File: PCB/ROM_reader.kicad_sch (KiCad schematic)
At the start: 37 parts, among them J1 TTL_UART, J2 USB_B_Mini, J3 ISP, U1 CH340G, U2 ATmega128A-A, Y1 12MHz

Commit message: ROM reader project PCBs updated
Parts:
- removed C11: 100u, Capacitor_SMD:CP_Elec_8x5.4, symbol Device:C_Polarized
- removed L1, L2: 100u, Inductor_SMD:L_1812_4532Metric_Pad1.30x3.40mm_HandSolder, symbol Device:L
- removed R5: 10M, Resistor_SMD:R_1206_3216Metric_Pad1.30x1.75mm_HandSolder, symbol Device:R
- added D1: Schottky, Diode_SMD:D_SMB_Handsoldering, symbol Device:D_Schottky
- added H1, H2, H3, H4: MH, MountingHole:MountingHole_3.2mm_M3_DIN965, symbol Mechanical:MountingHole
- added J4: EC, Connector_PinHeader_2.54mm:PinHeader_1x02_P2.54mm_Vertical, symbol Connector:Conn_01x02_Pin
- F1: footprint Fuse:Fuse_2010_5025Metric_Pad1.52x2.65mm_HandSolder -> Fuse:Fuse_2512_6332Metric_Pad1.52x3.35mm_HandSolder
- R2, R3: value 10k -> 1k5
- Y?: value 12MHz -> 7.3782MHz
- renumbered C14 to C13, D1 to D2, D2 to D3, D3 to D4, J2 to J1, J1 to J2
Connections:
- net AVCC is gone; now on net +5V: C5.1, C8.1, U2.64 (AVCC)
- net +5V: now also D1.1 (K)
- net GND: now also D1.2 (A)
- net #WR: now reaches U2.33 (PG0)
- net #WR: now also J4.1 (Pin_1)
- net A15_RAM_ADAPTER: now reaches U2.42 (PC7)
- net A15_RAM_ADAPTER: now also J4.2 (Pin_2)
- no-connect marks 27 -> 25
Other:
- note added: "U1 can be: CH340G (Y1, C3, C6 necessary) or CH340C (Y1, C3, C6 not required)"
- moved on the sheet: C4, C?, D2, J2, J3, R?, SW?

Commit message: Minor changes in text placement on PCB, comments. Revision updated to B
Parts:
- D3, D4: footprint LED_SMD:LED_1206_3216Metric_Pad1.42x1.75mm_HandSolder -> LED_SMD:LED_2010_5025Metric_Pad1.52x2.65mm_HandSolder
- J4: value EC -> RAM ADAPTER EXT; footprint Connector_PinHeader_2.54mm:PinHeader_1x02_P2.54mm_Vertical -> Connector_PinHeader_2.54mm:PinHeader_1x02_P2.54mm_Horizontal
- J?: value DB25_Plug -> ROM MODULE
- R2, R3: value 1k5 -> 2k2
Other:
- moved on the sheet: C10, C13, C5, C8, J4

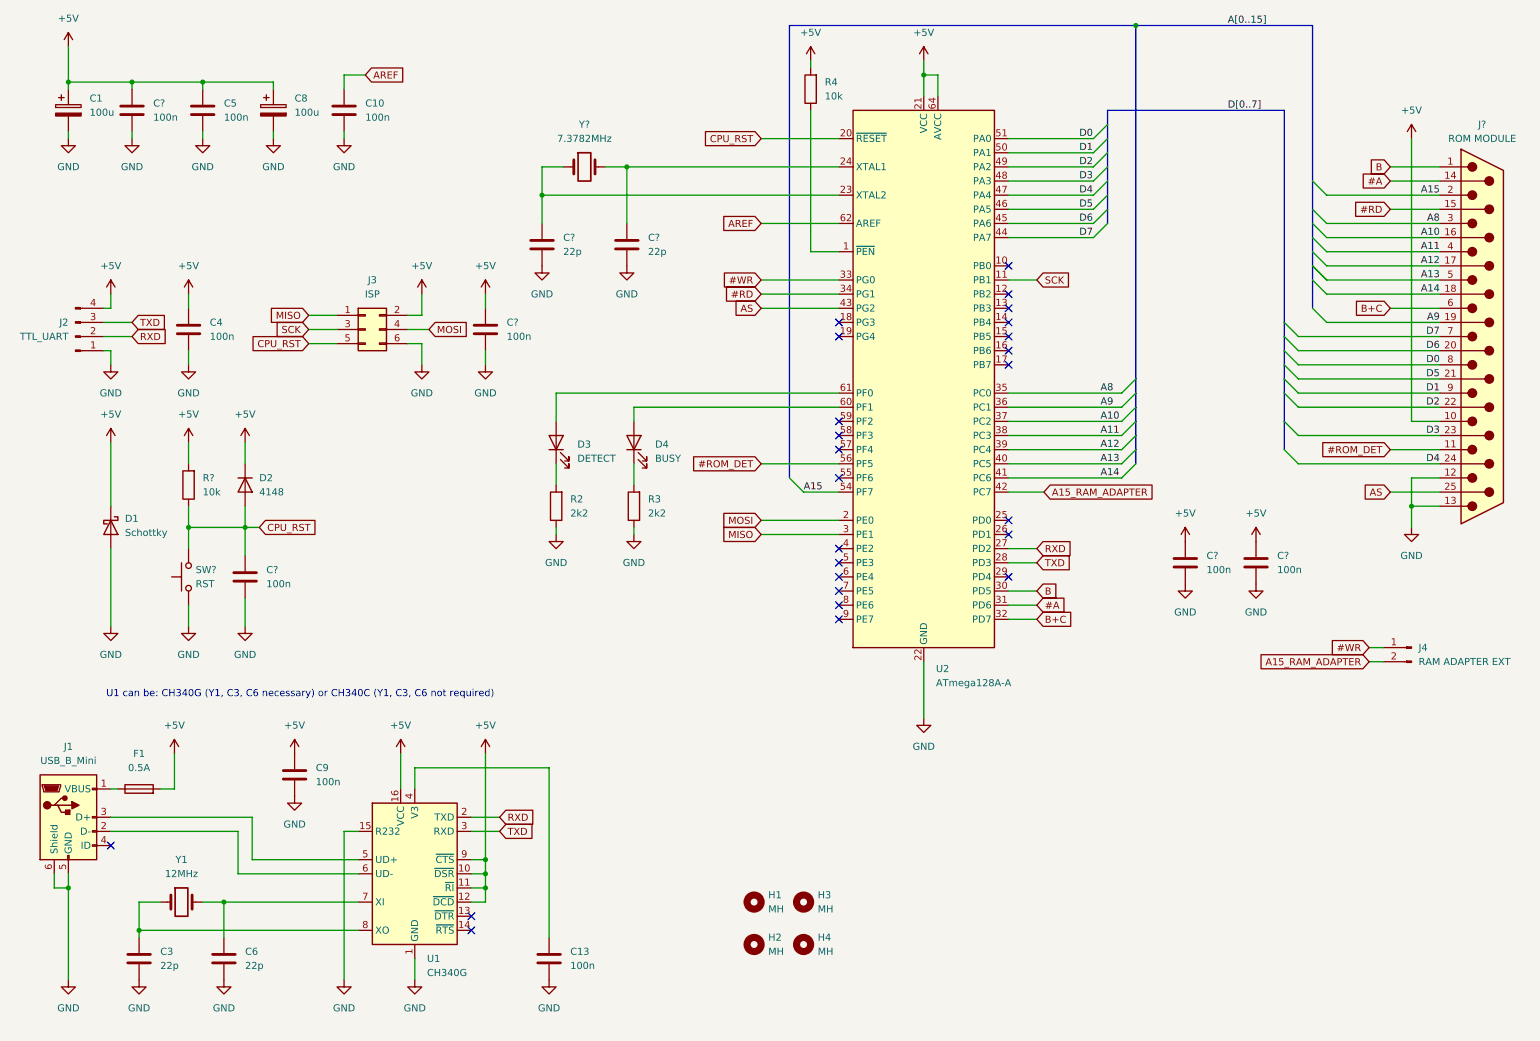
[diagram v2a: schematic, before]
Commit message: PCB project update: pull-up resistors added for D0-D7 data lines
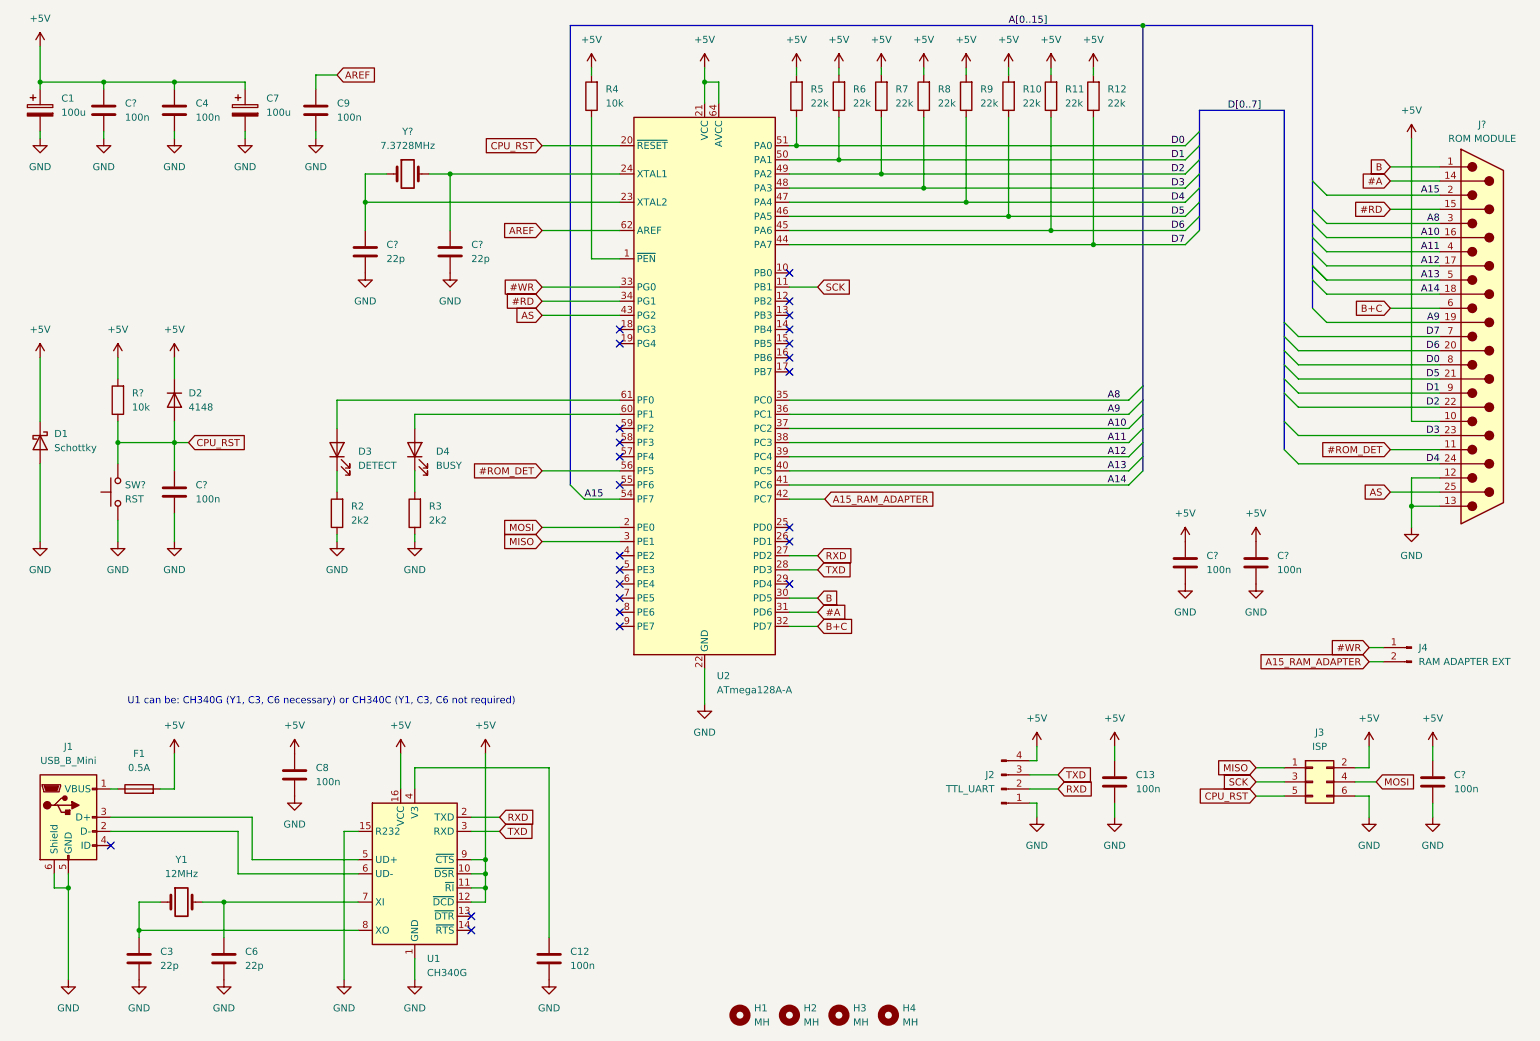
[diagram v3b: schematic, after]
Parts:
- added R10, R11, R12, R5, R6, R7, R8, R9: 22k, Resistor_SMD:R_1206_3216Metric_Pad1.30x1.75mm_HandSolder, symbol Device:R
- Y?: value 7.3782MHz -> 7.3728MHz
- renumbered C13 to C12, C4 to C13, C5 to C4, C8 to C7, C9 to C8, C10 to C9
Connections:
- net +5V: now also R10.2, R11.2, R12.2, R5.2, R6.2, R7.2, R8.2, R9.2
- net D0: now also R5.1
- net D1: now also R6.1
- net D2: now also R7.1
- net D3: now also R8.1
- net D4: now also R9.1
- net D5: now also R10.1
- net D6: now also R11.1
- net D7: now also R12.1
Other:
- moved on the sheet: C1, C13, C4, C7, C9, C?, D1, D2, D3, D4, H1, H2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

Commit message: Minor updates
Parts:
- C1, C7: footprint Capacitor_SMD:CP_Elec_8x5.4 -> Capacitor_SMD:CP_Elec_6.3x7.7
- D3, D4: footprint LED_SMD:LED_2010_5025Metric_Pad1.52x2.65mm_HandSolder -> LED_SMD:LED_1206_3216Metric_Pad1.42x1.75mm_HandSolder
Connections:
- net #WR: now also J4.2 (Pin_2); no longer J4.1 (Pin_1)
- net A15_RAM_ADAPTER: now also J4.1 (Pin_1); no longer J4.2 (Pin_2)
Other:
- title: FLT/CU1 ROM reader -> FLT/ART/CU-1 ROM reader
- moved on the sheet: J4
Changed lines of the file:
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@@
 	(paper "A4")
 	(title_block
-		(title "FLT/CU1 ROM reader")
-		(date "2025-01-31")
+		(title "FLT/ART/CU-1 ROM reader")
+		(date "2025-02-10")
 		(rev "C")
 		(company "trwgQ26xxx")
@@
 	(wire
 		(pts
+			(xy 256.54 128.27) (xy 259.08 128.27)
+		)
+		(stroke
+			(width 0)
+			(type default)
+		)
+	)
+	(wire
+		(pts
 			(xy 53.34 168.91) (xy 74.93 168.91)
 		)
@@
 		)
 	)
-	(wire
-		(pts
-			(xy 256.54 130.81) (xy 259.08 130.81)
-		)
-		(stroke
-			(width 0)
-			(type default)
-		)
-	)
 	(bus
 		(pts
@@
 	(wire
 		(pts
+			(xy 256.54 130.81) (xy 259.08 130.81)
+		)
+		(stroke
+			(width 0)
+			(type default)
+		)
+	)
+	(wire
+		(pts
 			(xy 236.22 154.94) (xy 241.3 154.94)
 		)
@@
 	(wire
 		(pts
-			(xy 256.54 128.27) (xy 259.08 128.27)
-		)
-		(stroke
-			(width 0)
-			(type default)
-		)
-	)
-	(wire
-		(pts
 			(xy 31.75 91.44) (xy 41.91 91.44)
 		)
@@
 	(symbol
 		(lib_id "Connector:Conn_01x02_Pin")
-		(at 264.16 128.27 0)
-		(mirror y)
+		(at 264.16 130.81 180)
 		(unit 1)
 		(exclude_from_sim no)
@@
 		(dnp no)
 		(property "Reference" "J4"
-			(at 265.43 128.2699 0)
+			(at 265.43 130.8101 0)
 			(effects
 				(font
@@
 		)
 		(property "Value" "RAM ADAPTER EXT"
-			(at 265.43 130.8099 0)
+			(at 265.43 128.2701 0)
 			(effects
 				(font
@@
 		)
 		(property "Footprint" "Connector_PinHeader_2.54mm:PinHeader_1x02_P2.54mm_Horizontal"
-			(at 264.16 128.27 0)
+			(at 264.16 130.81 0)
 			(effects
 				(font
@@
 		)
 		(property "Datasheet" "~"
-			(at 264.16 128.27 0)
+			(at 264.16 130.81 0)
 			(effects
 				(font
@@
 		)
 		(property "Description" "Generic connector, single row, 01x02, script generated"
-			(at 264.16 128.27 0)
+			(at 264.16 130.81 0)
 			(effects
 				(font
@@
 			)
 		)
-		(property "Footprint" "LED_SMD:LED_2010_5025Metric_Pad1.52x2.65mm_HandSolder"
+		(property "Footprint" "LED_SMD:LED_1206_3216Metric_Pad1.42x1.75mm_HandSolder"
 			(at 71.12 92.71 0)
 			(effects
@@
 			)
 		)
-		(property "Footprint" "Capacitor_SMD:CP_Elec_8x5.4"
+		(property "Footprint" "Capacitor_SMD:CP_Elec_6.3x7.7"
 			(at 55.5752 35.56 0)
 			(effects
@@
 			)
 		)
-		(property "Footprint" "Capacitor_SMD:CP_Elec_8x5.4"
+		(property "Footprint" "Capacitor_SMD:CP_Elec_6.3x7.7"
 			(at 18.7452 35.56 0)
 			(effects
@@
 			)
 		)
-		(property "Footprint" "LED_SMD:LED_2010_5025Metric_Pad1.52x2.65mm_HandSolder"
+		(property "Footprint" "LED_SMD:LED_1206_3216Metric_Pad1.42x1.75mm_HandSolder"
 			(at 85.09 92.71 0)
 			(effects
